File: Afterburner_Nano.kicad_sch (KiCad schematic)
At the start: 15 parts, among them U4 ESP32-C6-MINI-1

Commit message: layout changes
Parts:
- added R29, R30: 22, Resistor_SMD:R_0201_0603Metric, symbol Device:R
- added R31: 3k3, Resistor_SMD:R_0201_0603Metric, symbol Device:R
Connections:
- net ALERT_INT: now also U4.20 (IO15); no longer U4.19 (IO14)
- net D+: now also R30.1; no longer U4.18 (IO13)
- net D-: now also R29.1; no longer U4.17 (IO12)
- net GND: now also R31.2
- net LOADCELL_CS: now also U4.30 (RXD0); no longer U4.28 (IO22)
- net LOADCELL_DRDY: now also U4.31 (TXD0); no longer U4.29 (IO23)
- net MISO: now also U4.29 (IO23); no longer U4.27 (IO21)
- net MOSI: now also U4.28 (IO22); no longer U4.26 (IO20)
- net SCK: now also U4.27 (IO21); no longer U4.25 (IO19)
- net SCL: now also U4.25 (IO19); no longer U4.22 (IO8)
- net SDA: now also U4.24 (IO18); no longer U4.20 (IO15)
- net TEMP_CS: now also U4.26 (IO20); no longer U4.24 (IO18)
- new net ESP-D+: R30.2, U4.18 (IO13)
- new net ESP-D-: R29.2, U4.17 (IO12)
- new net GPIO8: R31.1, U4.22 (IO8)

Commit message: layout changes
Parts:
- added C20, C21: 4.7u, Capacitor_SMD:C_0603_1608Metric, symbol Device:C
- added IC8: AP7361E-33FGE-7, Footprints:SON65P300X300X63-9N, symbol Symbols:AP7361E-33FGE-7
- added IC9: LM66200DRLR, Footprints:SOTFL50P160X60-8N, symbol Symbols:LM66200DRLR
- added R32: 1k, Resistor_SMD:R_0201_0603Metric, symbol Device:R
- added R33: 10k, Resistor_SMD:R_0201_0603Metric, symbol Device:R
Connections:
- net +3V3: now also C21.1, IC8.1 (OUT)
- net GND: now also C20.2, C21.2, IC8.4 (GND_1), IC8.9 (GND_2), IC9.1 (GND_1), IC9.5 (GND_2), R32.2
- new net: IC9.4 (~{ON}), R32.1
- new net: IC9.8 (ST), R33.1
- new net +5V: IC9.6 (VIN2)
- new net +5V_LDO: C20.1, IC8.5 (EN), IC8.8 (IN), IC9.2 (VOUT_1), IC9.7 (VOUT_2)
- new net VBUS_COM_CONNECTOR: IC9.3 (VIN1), R33.2
- no-connect marks 0 -> 5
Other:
- sheet CONNECTOR ports: added CC1, CC2, VBUS; removed none
- note added: "I2C address = 0x20"
- note added: "I2C address = 0x40"
- note added: "LDO 3V 1A"
- note added: "POWER SWITCHING"

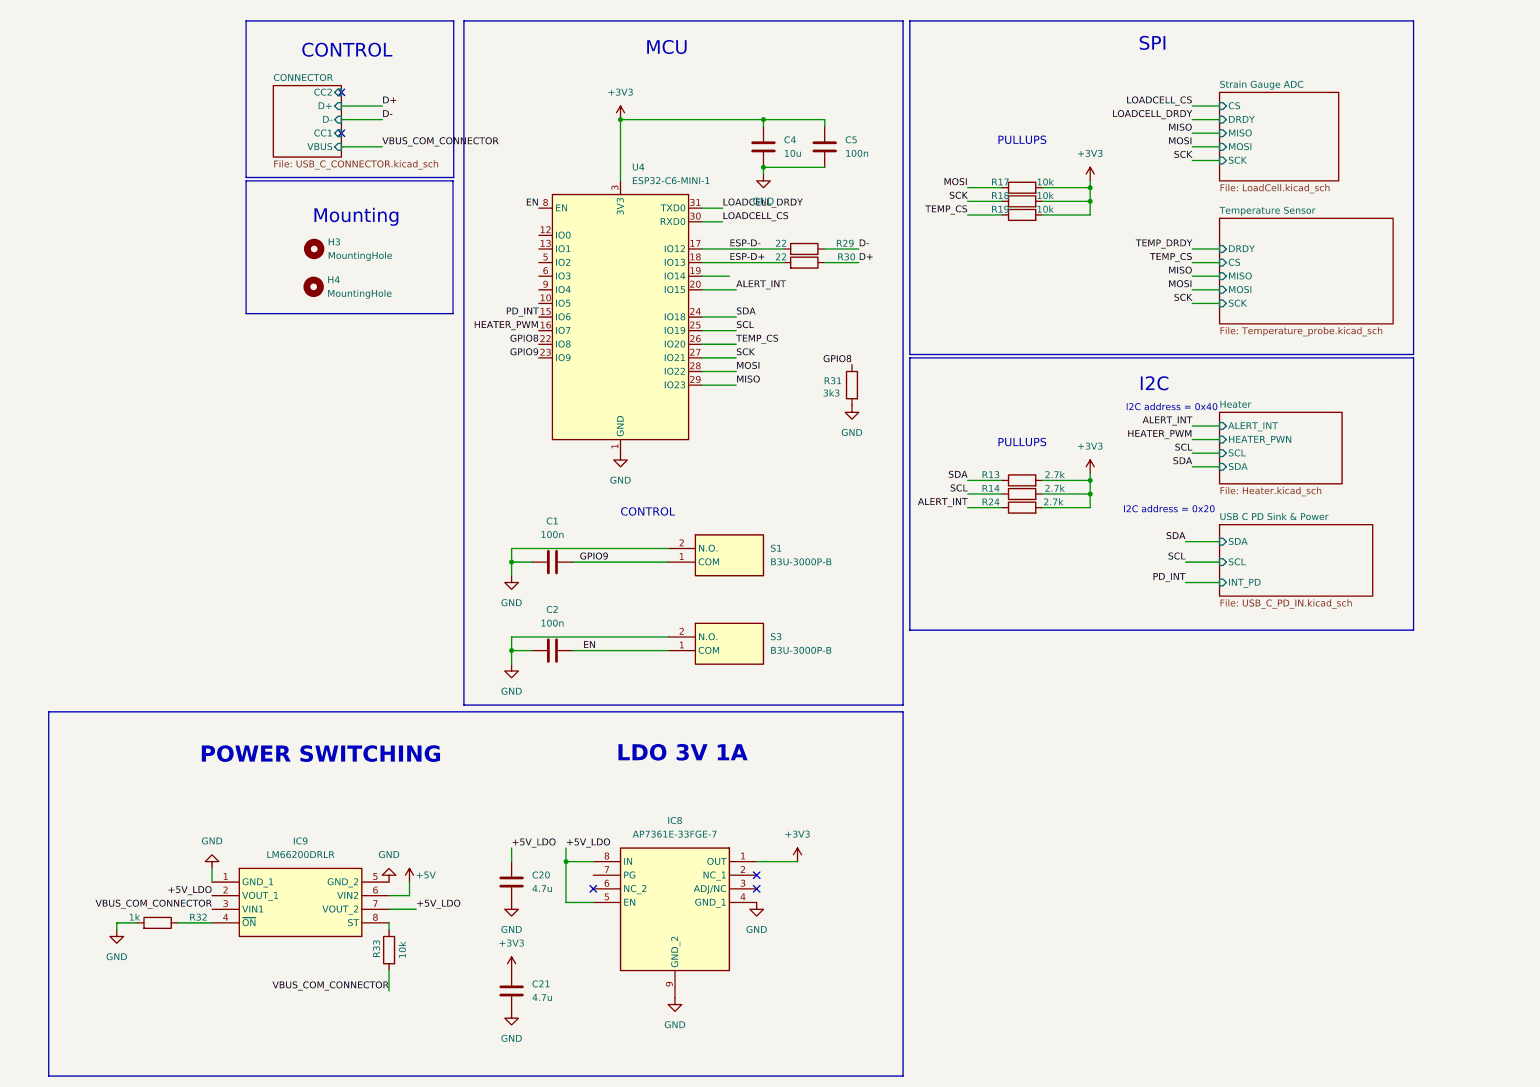
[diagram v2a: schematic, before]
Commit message: Power layout changes
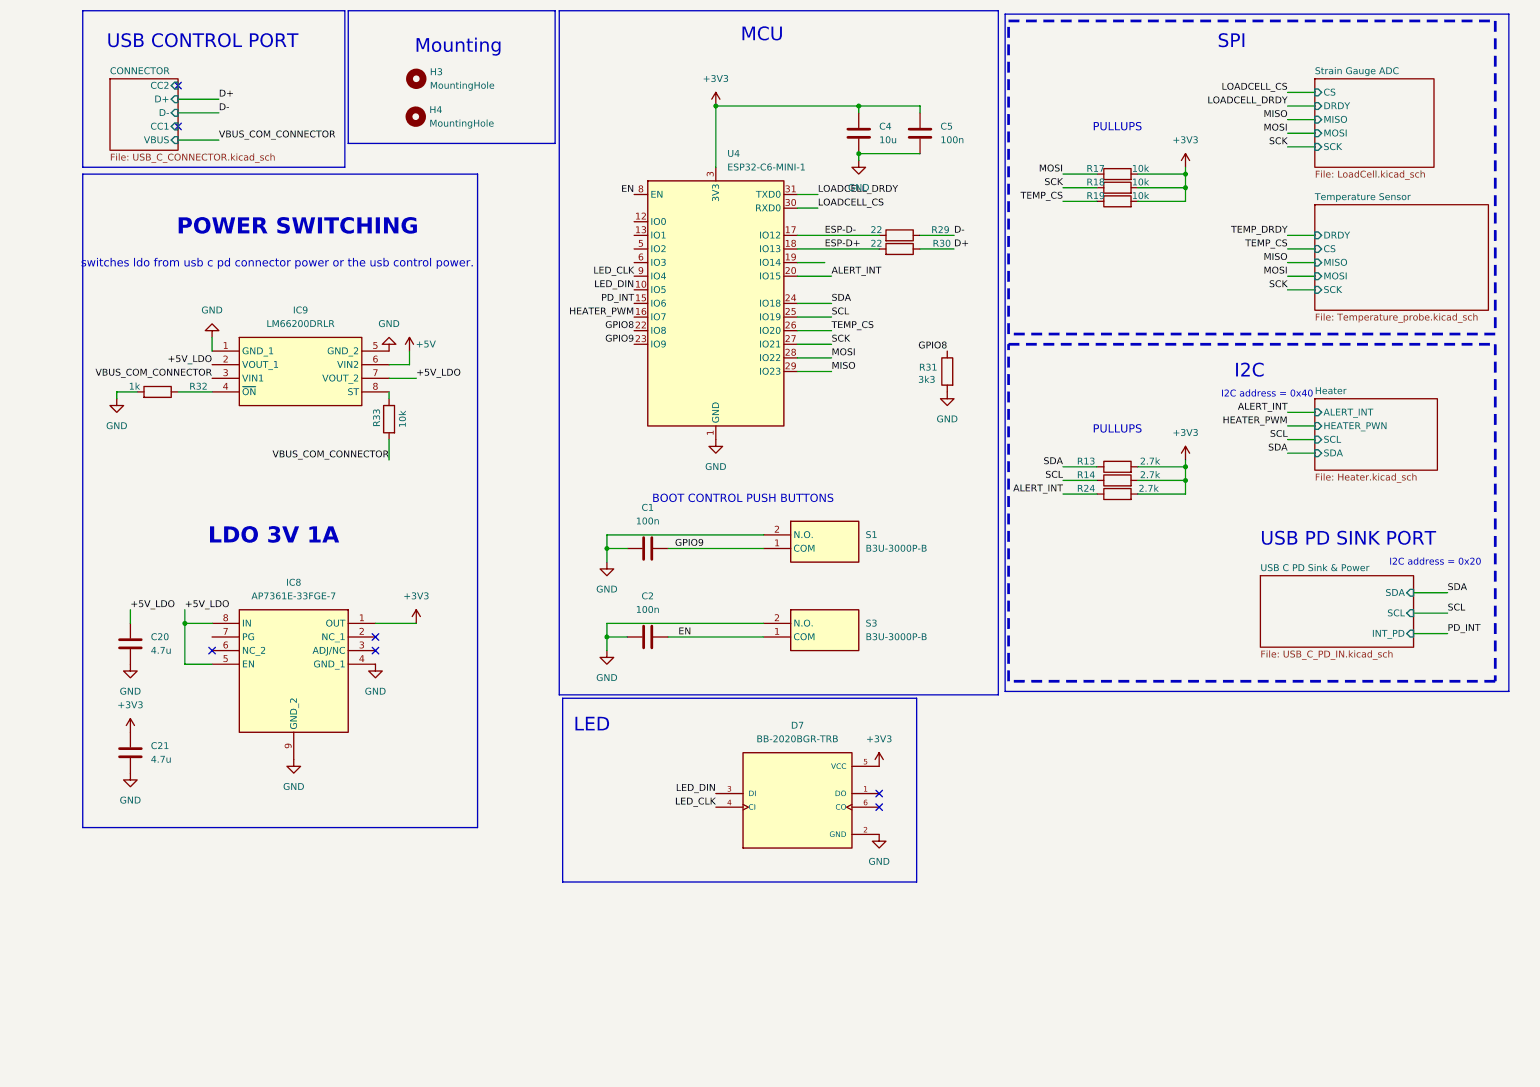
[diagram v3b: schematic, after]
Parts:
- added D7: BB-2020BGR-TRB, Footprints:LED_BB-2020BGR-TRB, symbol Symbols:BB-2020BGR-TRB
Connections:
- net +3V3: now also D7.5 (VCC)
- net GND: now also D7.2 (GND)
- net LED_DIN: now reaches U4.10 (IO5)
- net LED_DIN: now also D7.3 (DI)
- net LED_CLK: now reaches U4.9 (IO4)
- net LED_CLK: now also D7.4 (CI)
- no-connect marks 5 -> 7
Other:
- note added: "BOOT CONTROL PUSH BUTTONS"
- note added: "LED"
- note added: "USB CONTROL PORT"
- note added: "USB PD SINK PORT"
- note added: "switches ldo from usb c pd connector power or the usb control power."
- note removed: "CONTROL"
- moved on the sheet: C1, C2, C20, C21, C4, C5, H3, H4, IC8, IC9, R13, R14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

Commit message: Layout Changes, MPN Added
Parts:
- C20, C21: MPN (none) -> GPC0603475-10
- C5: GPN GPC0402104-16 -> (none); MPN (none) -> GPC0402104-25
- IC8: MPN (none) -> AP7361E-33FGE-7
- IC9: MPN (none) -> LM66200DRLR
- R13, R14, R24: GPN GPR04022K7 -> (none); MPN (none) -> GPR04022K7
- R17, R18, R19, R33: GPN GPR020110K -> (none); MPN (none) -> GPR020110K
- R29, R30: GPN GPR020110K -> (none); MPN (none) -> 0201WMF220JTEE
- R31: footprint Resistor_SMD:R_0201_0603Metric -> Resistor_SMD:R_0402_1005Metric; GPN GPR020110K -> (none); MPN (none) -> GPR04023K3
- R32: footprint Resistor_SMD:R_0201_0603Metric -> Resistor_SMD:R_0402_1005Metric; GPN GPR02011K -> (none); MPN (none) -> GPR04021K

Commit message: change res to correct size
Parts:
- R13, R14, R24: footprint Resistor_SMD:R_0201_0603Metric -> Resistor_SMD:R_0402_1005Metric
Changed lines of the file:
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@@
 			)
 		)
-		(property "Footprint" "Resistor_SMD:R_0201_0603Metric"
+		(property "Footprint" "Resistor_SMD:R_0402_1005Metric"
 			(at 210.82 103.378 90)
 			(effects
@@
 			)
 		)
-		(property "Footprint" "Resistor_SMD:R_0201_0603Metric"
+		(property "Footprint" "Resistor_SMD:R_0402_1005Metric"
 			(at 210.82 105.918 90)
 			(effects
@@
 			)
 		)
-		(property "Footprint" "Resistor_SMD:R_0201_0603Metric"
+		(property "Footprint" "Resistor_SMD:R_0402_1005Metric"
 			(at 210.82 100.838 90)
 			(effects
